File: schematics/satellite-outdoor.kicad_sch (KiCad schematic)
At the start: 3 parts, among them U1 LPS22HB, U2 AHT20

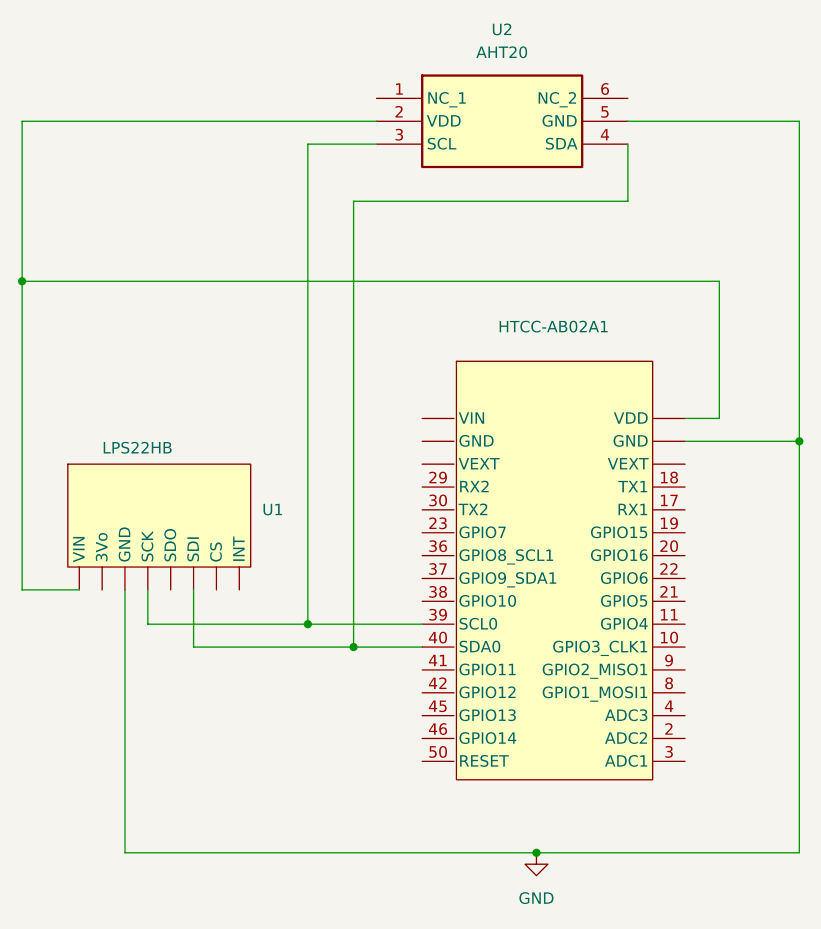
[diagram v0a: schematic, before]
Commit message: Schematics update: use Vext instead of VDD
Vext can be controllled and switched on/off.
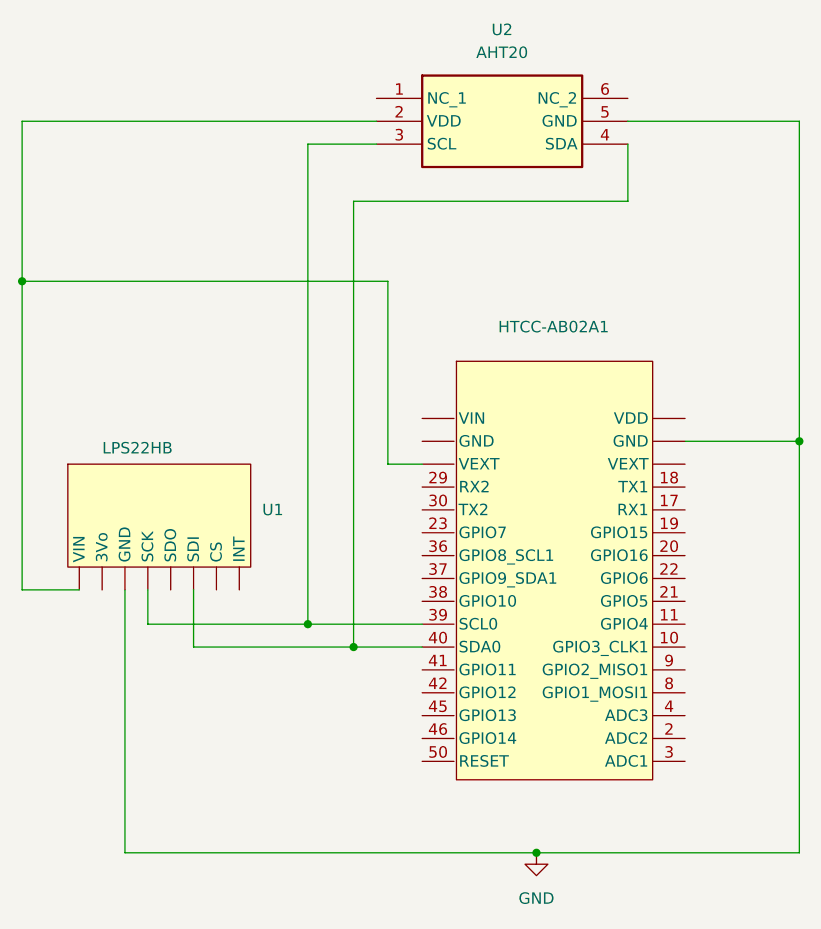
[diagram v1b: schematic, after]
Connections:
- new net: HTCC-AB02A1. (VIN), U1. (VIN), U2.2 (VDD)
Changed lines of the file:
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@@
 	(wire
 		(pts
-			(xy 72.39 64.77) (xy 149.86 64.77)
+			(xy 72.39 64.77) (xy 113.03 64.77)
 		)
 		(stroke
@@
 	(wire
 		(pts
-			(xy 146.05 80.01) (xy 149.86 80.01)
+			(xy 113.03 85.09) (xy 113.03 64.77)
 		)
 		(stroke
@@
 	(wire
 		(pts
-			(xy 149.86 64.77) (xy 149.86 80.01)
+			(xy 116.84 85.09) (xy 113.03 85.09)
 		)
 		(stroke
